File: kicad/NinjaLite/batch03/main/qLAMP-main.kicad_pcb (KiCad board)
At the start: 2 copper layers, 142 x 58 mm, 131 parts, among them J1 ALI_USB, J13 Conn_01x01_Male, J16 Conn_01x01_Male, J2 Barrel_Jack_Switch, J23 Conn_01x01_Male, J24 Conn_01x02_Male, J25 Conn_01x02_Male, J26 Conn_01x02_Male, J27 Conn_01x02_Male, J3 Conn_01x07_Male, J4 Conn_01x02_Male, J5 Conn_01x02_Male, Q1 Q_NMOS_GSD, Q3 Q_NMOS_GSD, Q5 Q_NMOS_GSD, U1 NAU7802, U10 TLC5929, U11 IP2721, U12 NE555, U13 LM393, U14 TCR3DF33,LM(CT, U17 LITE_LCD, U19 CD74HC4067M96, U2 NAU7802, U3 BD433M5FP-CE2, U4 LMP7717MF_NOPB, U5 ESP32-WROOM-32, U6 BA178M05FP-E2, U8 TS12A12511DCNR, U9 SN74LV4051A

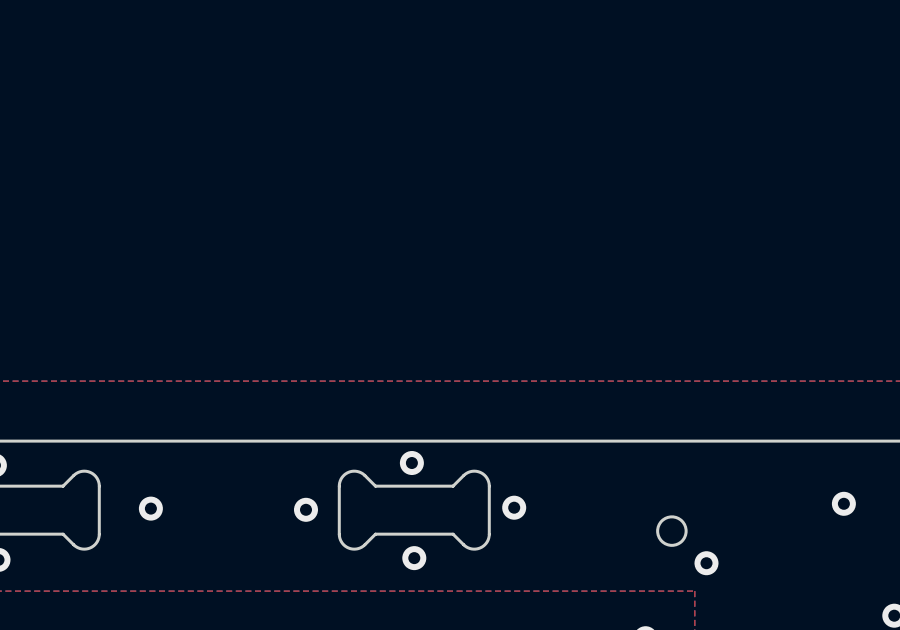
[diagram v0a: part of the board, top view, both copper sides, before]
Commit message: add batch03 and batch02/pdf
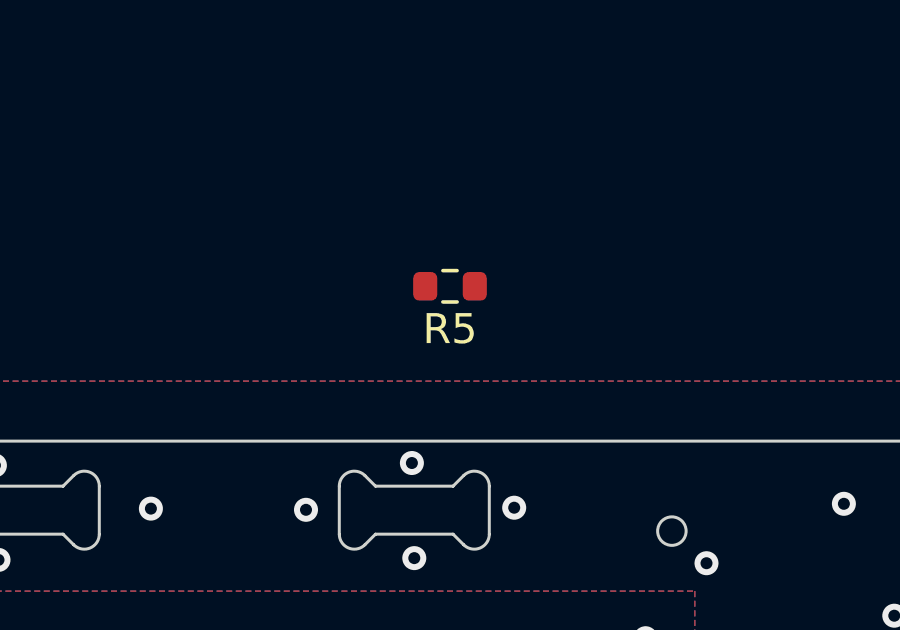
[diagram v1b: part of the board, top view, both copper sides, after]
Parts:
- added R5: 100k, Resistor_SMD:R_0603_1608Metric, F.Cu at (140.8, 67.8)
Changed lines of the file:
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@@
+    )
+  )
+  (footprint "Resistor_SMD:R_0603_1608Metric" (layer "F.Cu")
+    (at 140.84 67.84 180)
+    (descr "Resistor SMD 0603 (1608 Metric), square (rectangular) end terminal, IPC_7351 nominal, (Body size source: IPC-SM-782 page 72, https://www.pcb-3d.com/wordpress/wp-content/uploads/ipc-sm-782a_amendment_1_and_2.pdf), generated with kicad-footprint-generator")
+    (tags "resistor")
+    (property "Sheetfile" "filePower.kicad_sch")
+    (property "Sheetname" "Power")
+    (attr smd)
+    (fp_text reference "R5" (at 0 -1.43) (layer "F.SilkS")
+      (effects (font (size 1 1) (thickness 0.15)))
+    )
+    (fp_text value "100k" (at 0 1.43) (layer "F.Fab")
+      (effects (font (size 1 1) (thickness 0.15)))
+    )
+    (fp_text user "${REFERENCE}" (at 0 0) (layer "F.Fab")
+      (effects (font (size 0.4 0.4) (thickness 0.06)))
+    )
+    (fp_line (start -0.237258 0.5225) (end 0.237258 0.5225) (layer "F.SilkS") (width 0.12))
+    (fp_line (start -0.237258 -0.5225) (end 0.237258 -0.5225) (layer "F.SilkS") (width 0.12))
+    (fp_line (start -1.48 0.73) (end -1.48 -0.73) (layer "F.CrtYd") (width 0.05))
+    (fp_line (start 1.48 -0.73) (end 1.48 0.73) (layer "F.CrtYd") (width 0.05))
+    (fp_line (start -1.48 -0.73) (end 1.48 -0.73) (layer "F.CrtYd") (width 0.05))
+    (fp_line (start 1.48 0.73) (end -1.48 0.73) (layer "F.CrtYd") (width 0.05))
+    (fp_line (start 0.8 0.4125) (end -0.8 0.4125) (layer "F.Fab") (width 0.1))
+    (fp_line (start -0.8 -0.4125) (end 0.8 -0.4125) (layer "F.Fab") (width 0.1))
+    (fp_line (start -0.8 0.4125) (end -0.8 -0.4125) (layer "F.Fab") (width 0.1))
+    (fp_line (start 0.8 -0.4125) (end 0.8 0.4125) (layer "F.Fab") (width 0.1))
+    (pad "1" smd roundrect (at -0.825 0 180) (size 0.8 0.95) (layers "F.Cu" "F.Paste" "F.Mask") (roundrect_rratio 0.25)
+      (net 3 "3V3D") (pintype "passive"))
+    (pad "2" smd roundrect (at 0.825 0 180) (size 0.8 0.95) (layers "F.Cu" "F.Paste" "F.Mask") (roundrect_rratio 0.25)
+      (net 146 "/Power/RST-1V") (pintype "passive"))
+    (model "${KICAD6_3DMODEL_DIR}/Resistor_SMD.3dshapes/R_0603_1608Metric.wrl"
+      (offset (xyz 0 0 0))
+      (scale (xyz 1 1 1))
+      (rotate (xyz 0 0 0))
     )
   )

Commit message: just before ripup batch03/main
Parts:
- removed C16: 0.1uF, Capacitor_SMD:C_0603_1608Metric
- removed C18: DNP, Capacitor_SMD:C_0402_1005Metric
- removed C19: 3300pF, Capacitor_SMD:C_0603_1608Metric
- removed C20, C21: 10uF, Capacitor_SMD:C_0805_2012Metric
- removed D2, D3: D_Schottky, Ninja-qPCR:MSS1P3L-M3&slash_89A
- removed J5: Conn_01x02_Male, Connector_PinHeader_1.27mm:PinHeader_1x02_P1.27mm_Vertical
- removed JP3, JP4: Jumper_3_Open, Jumper:SolderJumper-3_P2.0mm_Open_TrianglePad1.0x1.5mm
- removed R12, R15, R25: 10k, Resistor_SMD:R_0603_1608Metric
- removed R14: 0.1k, Resistor_SMD:R_0603_1608Metric
- removed R24: 51k, Resistor_SMD:R_0603_1608Metric
- removed U12: NE555, Package_SO:SOIC-8_3.9x4.9mm_P1.27mm
- removed U13: LM393, Package_SO:SOIC-8_3.9x4.9mm_P1.27mm
- J4: footprint Connector_PinHeader_1.27mm:PinHeader_1x02_P1.27mm_Vertical -> Connector_PinHeader_2.54mm:PinHeader_1x02_P2.54mm_Vertical
- R13: value 20M -> 10M
- R5: value 100k -> 10M
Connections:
- C17 pad 1: 20V -> VCC
- C23 pad 1: 20V -> VCC
- C25 pad 1: 20V -> VCC
- C27 pad 1: 20V -> VCC
- C6 pad 1: Net-(C6-Pad1) -> /Photo/AMP_OUT
- D10A1 pad 1: Net-(D10A1-Pad1) -> VCC
- D10A1 pad 2: GNDA -> Net-(D10A1-Pad2)
- D10B1 pad 1: /PhotoMUX/S_PD_OUT3 -> Net-(D10A1-Pad2)
- D10B1 pad 2: Net-(D10A1-Pad1) -> /PhotoMUX/S_PD_OUT3
- D11A1 pad 1: Net-(D11A1-Pad1) -> VCC
- D11A1 pad 2: GNDA -> Net-(D11A1-Pad2)
- D11B1 pad 1: /PhotoMUX/S_PD_OUT5 -> Net-(D11A1-Pad2)
- D11B1 pad 2: Net-(D11A1-Pad1) -> /PhotoMUX/S_PD_OUT5
- D12A1 pad 1: Net-(D12A1-Pad1) -> VCC
- D12A1 pad 2: GNDA -> Net-(D12A1-Pad2)
- D12B1 pad 1: /PhotoMUX/S_PD_OUT7 -> Net-(D12A1-Pad2)
- D12B1 pad 2: Net-(D12A1-Pad1) -> /PhotoMUX/S_PD_OUT7
- D13A1 pad 1: Net-(D13A1-Pad1) -> VCC
- D13A1 pad 2: GNDA -> Net-(D13A1-Pad2)
- D13B1 pad 1: /PhotoMUX/S_PD_OUT9 -> Net-(D13A1-Pad2)
- D13B1 pad 2: Net-(D13A1-Pad1) -> /PhotoMUX/S_PD_OUT9
- D14A1 pad 1: Net-(D14A1-Pad1) -> VCC
- D14A1 pad 2: GNDA -> Net-(D14A1-Pad2)
- D14B1 pad 1: /PhotoMUX/S_PD_OUT11 -> Net-(D14A1-Pad2)
- D14B1 pad 2: Net-(D14A1-Pad1) -> /PhotoMUX/S_PD_OUT11
- D15A1 pad 1: Net-(D15A1-Pad1) -> VCC
- D15A1 pad 2: GNDA -> Net-(D15A1-Pad2)
- D15B1 pad 1: /PhotoMUX/S_PD_OUT13 -> Net-(D15A1-Pad2)
- D15B1 pad 2: Net-(D15A1-Pad1) -> /PhotoMUX/S_PD_OUT13
- D16A1 pad 1: Net-(D16A1-Pad1) -> VCC
- D16A1 pad 2: GNDA -> Net-(D16A1-Pad2)
- D16B1 pad 1: /PhotoMUX/S_PD_OUT15 -> Net-(D16A1-Pad2)
- D16B1 pad 2: Net-(D16A1-Pad1) -> /PhotoMUX/S_PD_OUT15
- D1A1 pad 1: Net-(D1A1-Pad1) -> VCC
- D1A1 pad 2: GNDA -> Net-(D1A1-Pad2)
- D1B1 pad 1: /PhotoMUX/N_PD_OUT1 -> Net-(D1A1-Pad2)
- D1B1 pad 2: Net-(D1A1-Pad1) -> /PhotoMUX/N_PD_OUT1
- D2A1 pad 1: Net-(D2A1-Pad1) -> VCC
- D2A1 pad 2: GNDA -> Net-(D2A1-Pad2)
- D2B1 pad 1: /PhotoMUX/N_PD_OUT3 -> Net-(D2A1-Pad2)
- D2B1 pad 2: Net-(D2A1-Pad1) -> /PhotoMUX/N_PD_OUT3
- D3A1 pad 1: Net-(D3A1-Pad1) -> VCC
- D3A1 pad 2: GNDA -> Net-(D3A1-Pad2)
- D3B1 pad 1: /PhotoMUX/N_PD_OUT5 -> Net-(D3A1-Pad2)
- D3B1 pad 2: Net-(D3A1-Pad1) -> /PhotoMUX/N_PD_OUT5
- D4A1 pad 1: Net-(D4A1-Pad1) -> VCC
- D4A1 pad 2: GNDA -> Net-(D4A1-Pad2)
- D4B1 pad 1: /PhotoMUX/N_PD_OUT7 -> Net-(D4A1-Pad2)
- D4B1 pad 2: Net-(D4A1-Pad1) -> /PhotoMUX/N_PD_OUT7
- D5A1 pad 1: Net-(D5A1-Pad1) -> VCC
- D5A1 pad 2: GNDA -> Net-(D5A1-Pad2)
- D5B1 pad 1: /PhotoMUX/N_PD_OUT9 -> Net-(D5A1-Pad2)
- D5B1 pad 2: Net-(D5A1-Pad1) -> /PhotoMUX/N_PD_OUT9
- D6A1 pad 1: Net-(D6A1-Pad1) -> VCC
- D6A1 pad 2: GNDA -> Net-(D6A1-Pad2)
- D6B1 pad 1: /PhotoMUX/N_PD_OUT11 -> Net-(D6A1-Pad2)
- D6B1 pad 2: Net-(D6A1-Pad1) -> /PhotoMUX/N_PD_OUT11
- D7A1 pad 1: Net-(D7A1-Pad1) -> VCC
- D7A1 pad 2: GNDA -> Net-(D7A1-Pad2)
- D7B1 pad 1: /PhotoMUX/N_PD_OUT13 -> Net-(D7A1-Pad2)
- D7B1 pad 2: Net-(D7A1-Pad1) -> /PhotoMUX/N_PD_OUT13
- D8A1 pad 1: Net-(D8A1-Pad1) -> VCC
- D8A1 pad 2: GNDA -> Net-(D8A1-Pad2)
- D8B1 pad 1: /PhotoMUX/N_PD_OUT15 -> Net-(D8A1-Pad2)
- D8B1 pad 2: Net-(D8A1-Pad1) -> /PhotoMUX/N_PD_OUT15
- D9A1 pad 1: Net-(D9A1-Pad1) -> VCC
- D9A1 pad 2: GNDA -> Net-(D9A1-Pad2)
- D9B1 pad 1: /PhotoMUX/S_PD_OUT1 -> Net-(D9A1-Pad2)
- D9B1 pad 2: Net-(D9A1-Pad1) -> /PhotoMUX/S_PD_OUT1
- HLID1 pad 1: 20V -> VCC
- HWELL1 pad 1: 20V -> VCC
- J2 pad 1: 20V -> VCC
- J24 pad 1: PD_MUX_OUT -> Net-(J24-Pad1)
- J25 pad 1: PD_MUX_OUT -> Net-(J24-Pad1)
- J4 pad 1: 3V3D -> PD_MUX_OUT
- J4 pad 2: Net-(J4-Pad2) -> /Photo/AMP_OUT
- JP6 pad 1: Net-(C6-Pad1) -> /Photo/AMP_OUT
- JP6 pad 2: /Photo/AMP_OUT -> unconnected-(JP6-Pad2)
- JP7 pad 1: Net-(C18-Pad1) -> /Photo/AMP_OUT
- Q1 pad 2: 20V -> VCC
- R13 pad 1: PD_MUX_OUT -> Net-(R13-Pad1)
- R13 pad 2: Net-(C6-Pad1) -> /Photo/AMP_OUT
- R16 pad 2: 20V -> VCC
- R19 pad 1: 20V -> VCC
- R5 pad 1: 3V3D -> PD_MUX_OUT
- R5 pad 2: /Power/RST-1V -> Net-(R13-Pad1)
- U11 pad 16: 20V -> VCC
- U19 pad 12: -1V -> GNDA
- U19 pad 15: -1V -> GNDA
- U3 pad 1: 20V -> VCC
- U4 pad 2: Net-(JP3-Pad2) -> GNDA
- U6 pad 1: 20V -> VCC
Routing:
- net /PhotoMUX/S_PD_OUT1: track 118.7 -> 4.60 mm
- net /PhotoMUX/S_PD_OUT3: track 113.8 -> 4.69 mm, vias 2 -> 0
- net /PhotoMUX/N_PD_OUT1: track 127.1 -> 19.8 mm, vias 1 -> 0
- net VCC: track 0.00 -> 107.1 mm
- net Net-(D9A1-Pad2): track 0.00 -> 98.9 mm
- net /PhotoMUX/N_PD_OUT3: track 117.8 -> 19.8 mm, vias 1 -> 0
- net /PhotoMUX/S_PD_OUT5: track 102.2 -> 4.61 mm, vias 2 -> 0
- net 20V: track 93.4 -> 0.00 mm
- net Net-(D10A1-Pad2): track 0.00 -> 89.5 mm
- net -1V: track 89.3 -> 0.00 mm, vias 4 -> 0
- net /PhotoMUX/S_PD_OUT7: track 93.5 -> 4.68 mm, vias 2 -> 0
- net /PhotoMUX/N_PD_OUT5: track 106.8 -> 19.6 mm, vias 1 -> 0
- net Net-(D1A1-Pad2): track 0.00 -> 84.9 mm
- net Net-(D11A1-Pad2): track 0.00 -> 80.0 mm
- net /PhotoMUX/N_PD_OUT7: track 99.1 -> 19.3 mm, vias 1 -> 0
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- added copper zone on F.Cu, net VCC
- removed copper zone on F.Cu, net 20V

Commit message: wiring batch03/main
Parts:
- moved R5 62.0 mm to (91.4, 105.3), turned to 0 degrees
- moved U2 44.6 mm to (106.0, 104.9), turned to 90 degrees
- moved J4 39.4 mm to (88.7, 104.8)
- moved U10 17.9 mm to (138.4, 101.4), turned to 180 degrees
- moved C33 15.5 mm to (127.2, 106.6), turned to 180 degrees
- moved C14 14.9 mm to (95.0, 99.2), turned to 90 degrees
- moved C10 13.0 mm to (136.6, 106.7), turned to 0 degrees
- moved R10 12.1 mm to (95.0, 102.3), turned to 0 degrees
- moved U14 11.5 mm to (127.3, 103.8), turned to 0 degrees
- moved R11 10.0 mm to (95.0, 103.8), turned to 0 degrees
- moved C1 8.86 mm to (95.0, 105.3)
- moved R2 8.49 mm to (140.4, 106.7), turned to 0 degrees
- moved C22 7.84 mm to (127.3, 100.9), turned to 0 degrees
- moved JP1 6.46 mm to (147.0, 119.5)
- moved C24 6.20 mm to (127.3, 98.9), turned to 0 degrees
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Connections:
- C6 pad 1: /Photo/AMP_OUT -> Net-(C6-Pad1)
- J24 pad 1: Net-(J24-Pad1) -> PD_MUX_OUT
- J25 pad 1: Net-(J24-Pad1) -> PD_MUX_OUT
- J4 pad 2: /Photo/AMP_OUT -> Net-(C6-Pad1)
- JP6 pad 1: /Photo/AMP_OUT -> Net-(C6-Pad1)
- JP6 pad 2: unconnected-(JP6-Pad2) -> /Photo/AMP_OUT
- R13 pad 2: /Photo/AMP_OUT -> Net-(C6-Pad1)
- U10 pad 10: /PhotoLED/S_LED_OUT2 -> /PhotoLED/S_LED_OUT6
- U10 pad 11: /PhotoLED/S_LED_OUT3 -> /PhotoLED/S_LED_OUT7
- U10 pad 12: /PhotoLED/S_LED_OUT4 -> /PhotoLED/S_LED_OUT8
- U10 pad 13: /PhotoLED/N_LED_OUT5 -> /PhotoLED/N_LED_OUT8
- U10 pad 14: /PhotoLED/N_LED_OUT6 -> /PhotoLED/N_LED_OUT7
- U10 pad 15: /PhotoLED/N_LED_OUT7 -> /PhotoLED/N_LED_OUT6
- U10 pad 16: /PhotoLED/N_LED_OUT8 -> /PhotoLED/N_LED_OUT5
- U10 pad 5: /PhotoLED/S_LED_OUT8 -> /PhotoLED/S_LED_OUT1
- U10 pad 6: /PhotoLED/S_LED_OUT7 -> /PhotoLED/S_LED_OUT2
- U10 pad 7: /PhotoLED/S_LED_OUT6 -> /PhotoLED/S_LED_OUT3
- U10 pad 8: /PhotoLED/S_LED_OUT5 -> /PhotoLED/S_LED_OUT4
- U10 pad 9: /PhotoLED/S_LED_OUT1 -> /PhotoLED/S_LED_OUT5
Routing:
- net GNDD: track 428.0 -> 74.9 mm, vias 20 -> 2
- net GNDA: track 346.2 -> 21.8 mm, vias 31 -> 2
- net 3V3D: track 294.3 -> 120.2 mm, vias 15 -> 4
- net 5V: track 152.3 -> 37.4 mm, vias 6 -> 0
- net VCC: track 107.1 -> 219.1 mm, vias 0 -> 2
- net /PhotoMUX/S_PD_OUT1: track 4.60 -> 115.9 mm
- net /PhotoMUX/N_PD_OUT1: track 19.8 -> 124.5 mm
- net /PhotoMUX/S_PD_OUT3: track 4.69 -> 106.0 mm
- net MUX_S1: track 191.3 -> 97.0 mm, vias 3 -> 1
- net /PhotoMUX/N_PD_OUT3: track 19.8 -> 113.9 mm
- net Net-(D9A1-Pad2): track 98.9 -> 6.17 mm
- net MUX_S0: track 185.4 -> 93.4 mm, vias 3 -> 1
- net /PhotoMUX/S_PD_OUT5: track 4.61 -> 95.7 mm
- net ADC_DRDY: track 87.3 -> 0.00 mm, vias 2 -> 0
- net /PhotoMUX/N_PD_OUT5: track 19.6 -> 103.2 mm
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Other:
- outline, holes or cut-outs redrawn

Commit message: wiring batch03/main done
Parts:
- added J5: Conn_01x01_Male, Pin_Headers:Pin_Header_Straight_1x01_Pitch1.27mm, B.Cu at (182.3, 119.2)
- added J6: Conn_01x01_Male, Pin_Headers:Pin_Header_Straight_1x01_Pitch1.27mm, B.Cu at (194.9, 100.1)
- added J7: Conn_01x01_Male, Pin_Headers:Pin_Header_Straight_1x01_Pitch1.27mm, B.Cu at (193.6, 100.1)
- J4: moved to F.Cu
- TEXT1, TEXT2, TEXT3: footprint Connector_PinHeader_2.54mm:PinHeader_1x02_P2.54mm_Vertical -> Pin_Headers:Pin_Header_Straight_1x02_Pitch1.27mm
- TLID1, TWELL1: footprint Connector_PinHeader_2.54mm:PinHeader_1x02_P2.54mm_Vertical -> Connector_Hirose:Hirose_DF13-02P-1.25DSA_1x02_P1.25mm_Vertical
- moved JP2 18.4 mm to (182.7, 129.3)
- moved R20 18.0 mm to (184.4, 98.8), turned to 0 degrees
- moved U9 17.8 mm to (162.7, 94.9), turned to -90 degrees
- moved R19 16.7 mm to (181.4, 98.8), turned to 0 degrees
- moved U3 9.08 mm to (166.0, 110.4)
- moved TAIR1 7.74 mm to (156.0, 91.9), turned to 180 degrees
- moved C31 7.57 mm to (163.9, 101.0)
- moved R17 7.25 mm to (156.7, 96.4), turned to -90 degrees
- moved R18 5.58 mm to (155.0, 96.4), turned to -90 degrees
- moved TWELL1 5.23 mm to (164.0, 86.8), turned to -90 degrees
- moved JP1 4.74 mm to (147.0, 124.3)
- moved U8 4.71 mm to (156.2, 100.2), turned to 90 degrees
- moved TLID1 3.78 mm to (159.6, 86.8), turned to -90 degrees
- moved R22 3.56 mm to (181.5, 122.9), turned to -90 degrees
- moved R23 3.56 mm to (185.0, 122.9), turned to -90 degrees
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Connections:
- U5 pad 28: ADC_DRDY -> Net-(U5-Pad28)
- U5 pad 6: unconnected-(U5-Pad6) -> Net-(U5-Pad6)
- U5 pad 7: unconnected-(U5-Pad7) -> Net-(U5-Pad7)
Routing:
- net GNDD: track 74.9 -> 346.6 mm, vias 2 -> 245
- net 5V: track 37.4 -> 242.7 mm, vias 0 -> 2
- net VCC: track 219.1 -> 416.9 mm, vias 2 -> 3
- net 3V3D: track 120.2 -> 285.4 mm, vias 4 -> 13
- net THERM_R_SWITCH: track 0.00 -> 88.7 mm, vias 0 -> 4
- net MUX_S2: track 99.4 -> 187.6 mm, vias 1 -> 3
- net MUX_S1: track 97.0 -> 182.3 mm, vias 1 -> 3
- net MUX_S0: track 93.4 -> 177.1 mm, vias 1 -> 3
- net LED: track 0.00 -> 81.2 mm, vias 0 -> 2
- net I2C_SCL: track 82.0 -> 161.4 mm, vias 1 -> 4
- net I2C_SDA: track 80.2 -> 158.4 mm, vias 1 -> 4
- net MUX_S3: track 98.9 -> 151.4 mm, vias 1 -> 2
- net LED_LAT: track 35.9 -> 87.4 mm, vias 1 -> 2
- net LED_SPI_SCLK: track 35.3 -> 84.4 mm, vias 1 -> 2
- net LED_SPI_MOSI: track 35.6 -> 80.8 mm, vias 1 -> 2
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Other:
- outline, holes or cut-outs redrawn
- board text removed: "3V3D"
- board text removed: "ADA4"
- board text removed: "ADA8"
- board text removed: "ADA_RST"
- board text removed: "CLKIN"
- board text removed: "GNDA"
- board text removed: "GNDD"
- board text removed: "INV"
- board text removed: "PASS"
- board text removed: "PD_REF_PWM"
- board text removed: "PN2"
- board text removed: "PP2"
